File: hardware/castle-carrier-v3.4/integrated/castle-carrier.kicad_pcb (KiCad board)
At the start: 4 copper layers, 100 x 80 mm, 104 parts, among them J1 PT 3.5 1x03, J10 DEBUG UART, J11 DC-005-5A, J12 BTN + PIXEL, J15 QWIIC I2C, J16 TYPE-C-31-M-12, J2 PT 3.5 1x03, J3 PT 3.5 1x03, J4 PT 3.5 1x03, J5 AM312 PIR, J7 SPEAKER L, J8 SPEAKER R, J9 DM3AT-SF-PEJM5, Q1 AOD4185, SW1 OS102011MS2Q, SW2 BOOT, SW3 RESET, U1 74AHCT125, U2 ESP32-S3-WROOM-1-N16R8, U3 AP63203WU-7, U4 USBLC6-2SC6, U5 INA219AIDCNR, U6 MAX98357AETE+T, U7 MAX98357AETE+T, U8 TPS22919DCKR

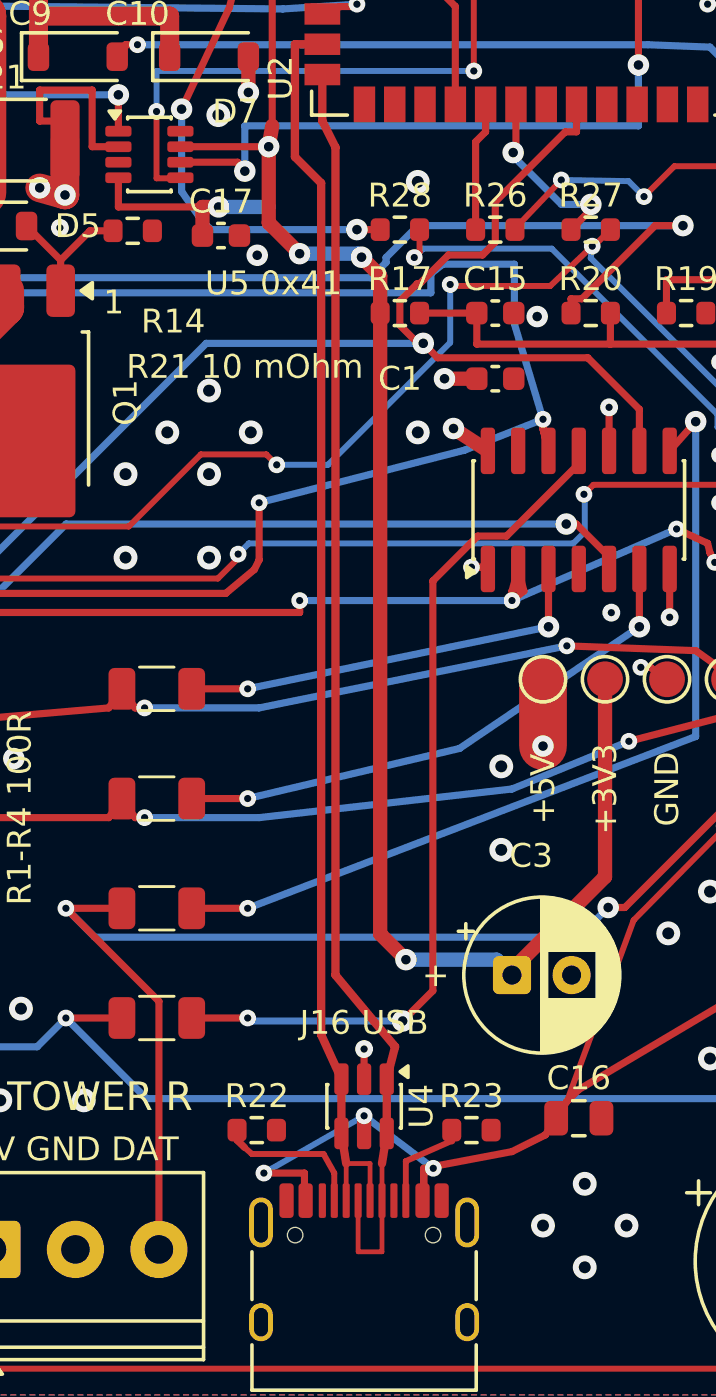
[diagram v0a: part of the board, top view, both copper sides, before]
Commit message: Validate v3.4 prototype handoff and tune USB routing
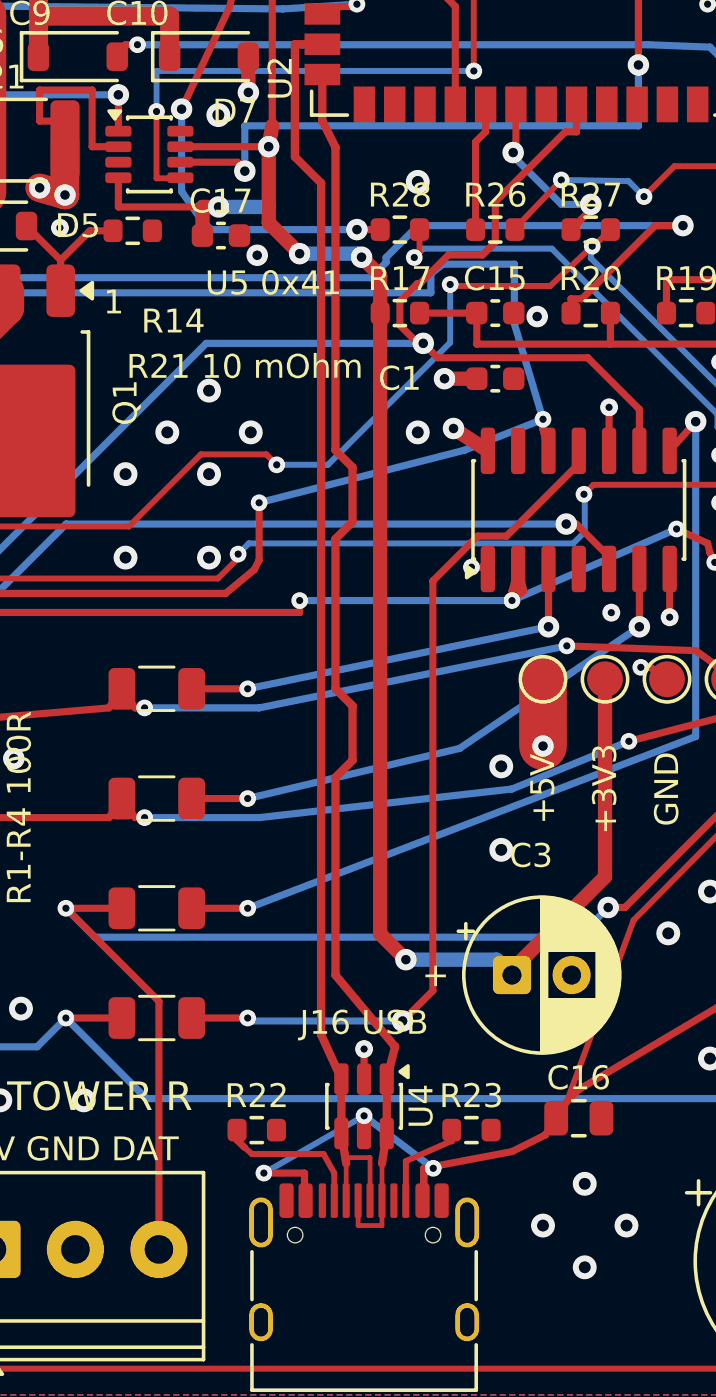
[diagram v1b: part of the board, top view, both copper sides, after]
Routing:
- net USB_DP: track 53.6 -> 52.6 mm
- net USB_DM: track 52.8 -> 53.3 mm
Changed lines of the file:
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@@
 	)
 	(segment
-		(start 111.75 113.6)
+		(start 109.8 93.71597)
+		(end 109.8 102)
+		(width 0.35)
+		(layer "F.Cu")
+		(net "USB_DP")
+	)
+	(segment
+		(start 111.75 112.5)
 		(end 111.75 111.455)
 		(width 0.2)
+		(layer "F.Cu")
+		(net "USB_DP")
+	)
+	(segment
+		(start 109.8 83.71597)
+		(end 109.8 90)
+		(width 0.35)
 		(layer "F.Cu")
 		(net "USB_DP")
@@
 	)
 	(segment
-		(start 110.75 113.6)
-		(end 111.75 113.6)
-		(width 0.2)
+		(start 110.75 112.5)
+		(end 111.75 112.5)
+		(width 0.2)
+		(layer "F.Cu")
+		(net "USB_DP")
+	)
+	(segment
+		(start 110.51597 80.71597)
+		(end 110.51597 83)
+		(width 0.35)
+		(layer "F.Cu")
+		(net "USB_DP")
+	)
+	(segment
+		(start 110.51597 90.71597)
+		(end 110.51597 93)
+		(width 0.35)
 		(layer "F.Cu")
 		(net "USB_DP")
@@
 	)
 	(segment
-		(start 109.8 102)
-		(end 109.8 67.3)
+		(start 109.8 90)
+		(end 110.51597 90.71597)
+		(width 0.35)
+		(layer "F.Cu")
+		(net "USB_DP")
+	)
+	(segment
+		(start 109.8 67.3)
+		(end 109.8 80)
 		(width 0.35)
 		(layer "F.Cu")
@@
 	)
 	(segment
+		(start 110.51597 83)
+		(end 109.8 83.71597)
+		(width 0.35)
+		(layer "F.Cu")
+		(net "USB_DP")
+	)
+	(segment
+		(start 109.8 80)
+		(end 110.51597 80.71597)
+		(width 0.35)
+		(layer "F.Cu")
+		(net "USB_DP")
+	)
+	(segment
 		(start 112.3 105)
 		(end 109.8 102)
@@
 	)
 	(segment
+		(start 110.51597 93)
+		(end 109.8 93.71597)
+		(width 0.35)
+		(layer "F.Cu")
+		(net "USB_DP")
+	)
+	(segment
 		(start 110.75 111.455)
-		(end 110.75 113.6)
+		(end 110.75 112.5)
 		(width 0.2)
 		(layer "F.Cu")
@@
 	)
 	(segment
+		(start 110.25 109.65)
+		(end 110.25 109.9)
+		(width 0.2)
+		(layer "F.Cu")
+		(net "USB_DM")
+	)
+	(segment
 		(start 108.1 67.7)
 		(end 109.2 68.8)
@@
 	)
 	(segment
-		(start 111.25 109.9)
+		(start 111.25 109.65)
 		(end 111.25 111.455)
 		(width 0.2)
@@
 	)
 	(segment
-		(start 110.25 109.9)
-		(end 111.25 109.9)
-		(width 0.2)
-		(layer "F.Cu")
+		(start 110.25 109.65)
+		(end 111.25 109.65)
+		(width 0.2)
+		(layer "F.Cu")
